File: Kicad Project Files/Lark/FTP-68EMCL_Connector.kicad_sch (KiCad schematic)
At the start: 6 parts, among them J4 B34B-PHDSS

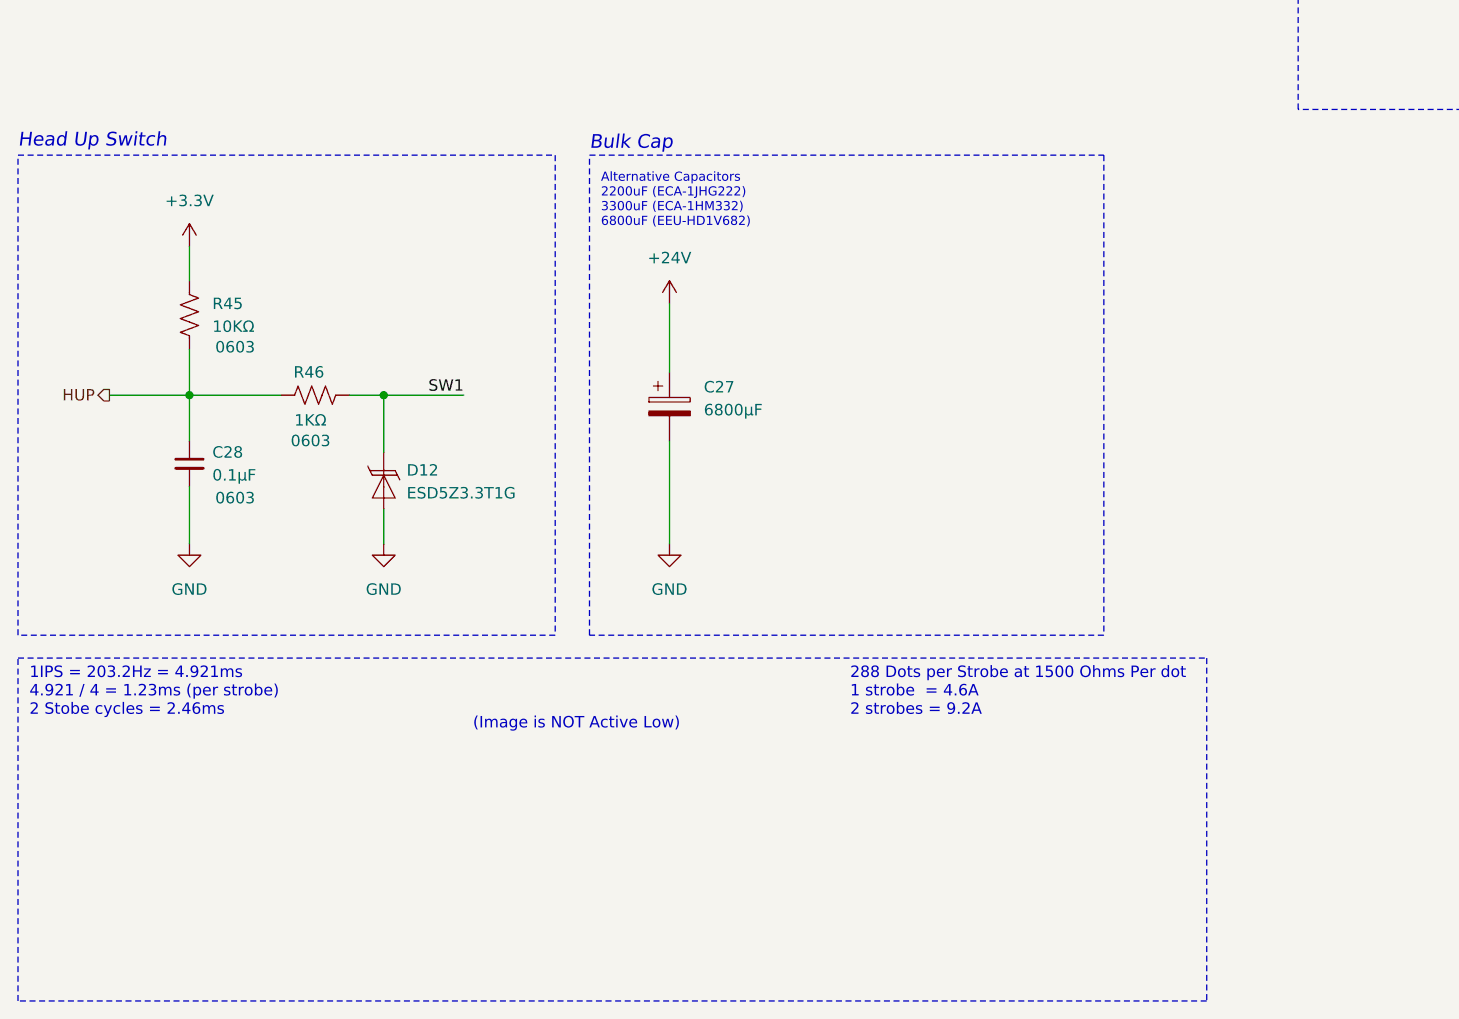
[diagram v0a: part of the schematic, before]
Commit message: fixed strobe timing image in schematic, now active low, as it should be
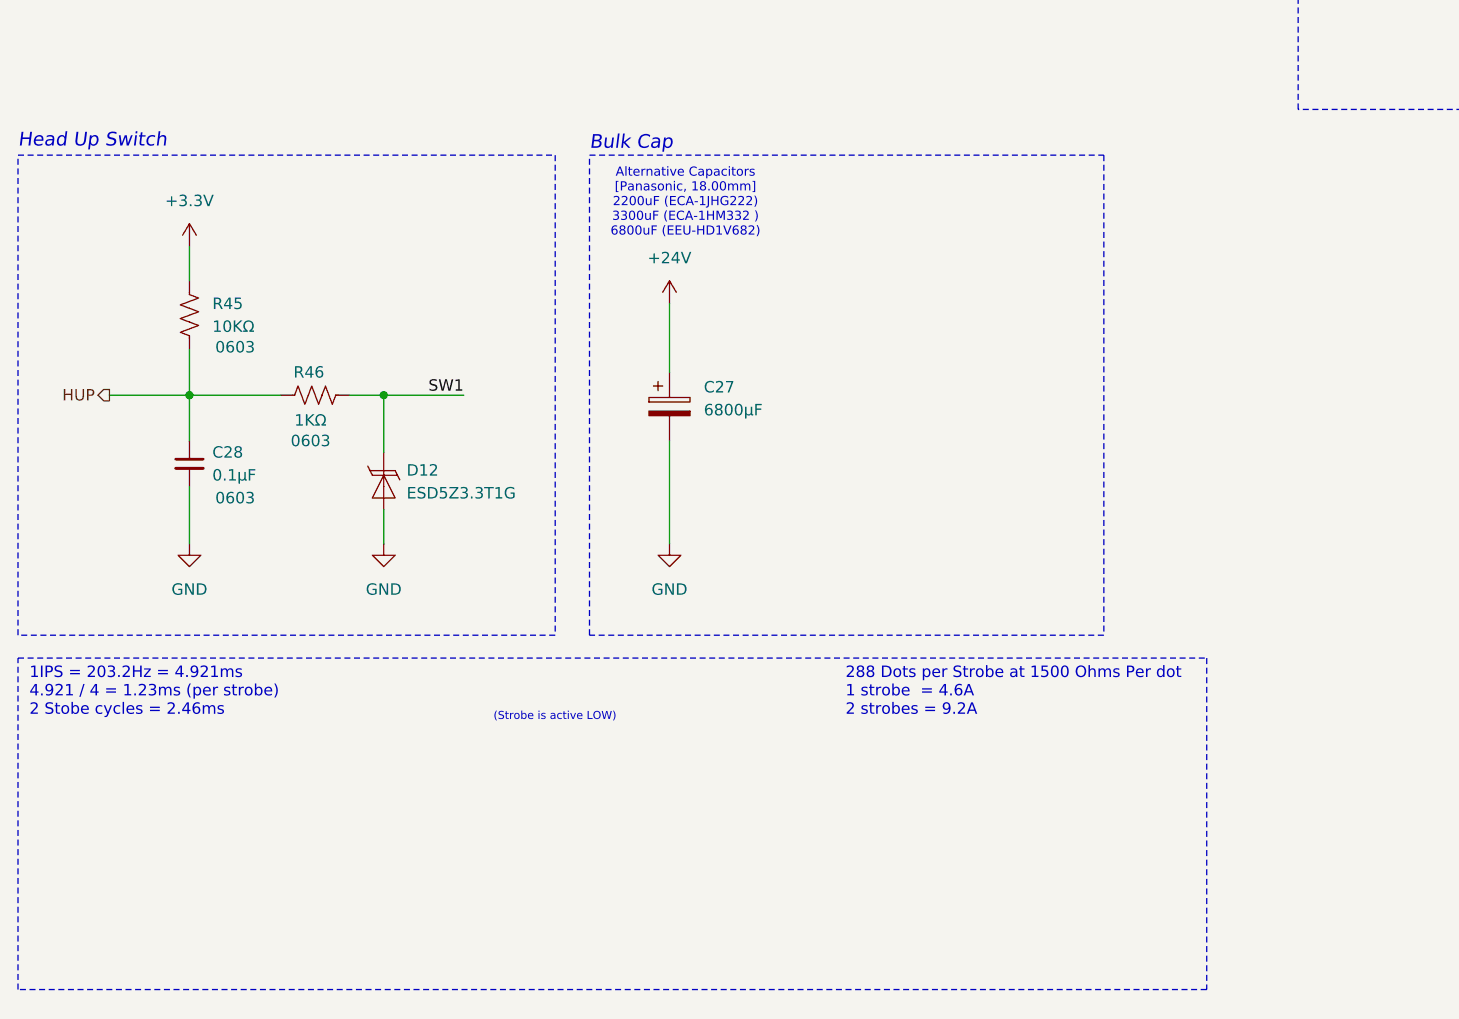
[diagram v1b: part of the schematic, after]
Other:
- note added: "(Strobe is active LOW)"
- note added: "Alternative Capacitors [Panasonic, 18.00mm] 2200uF (ECA-1JHG222) 3300uF (ECA-1HM332 ) 6800uF (EEU-HD1V682)"
- note removed: "(Image is NOT Active Low)"
- note removed: "Alternative Capacitors 2200uF (ECA-1JHG222) 3300uF (ECA-1HM332) 6800uF (EEU-HD1V682)"
